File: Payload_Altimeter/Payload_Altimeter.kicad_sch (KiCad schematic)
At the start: 1 part, among them U1 Arduino_Pro_Mini

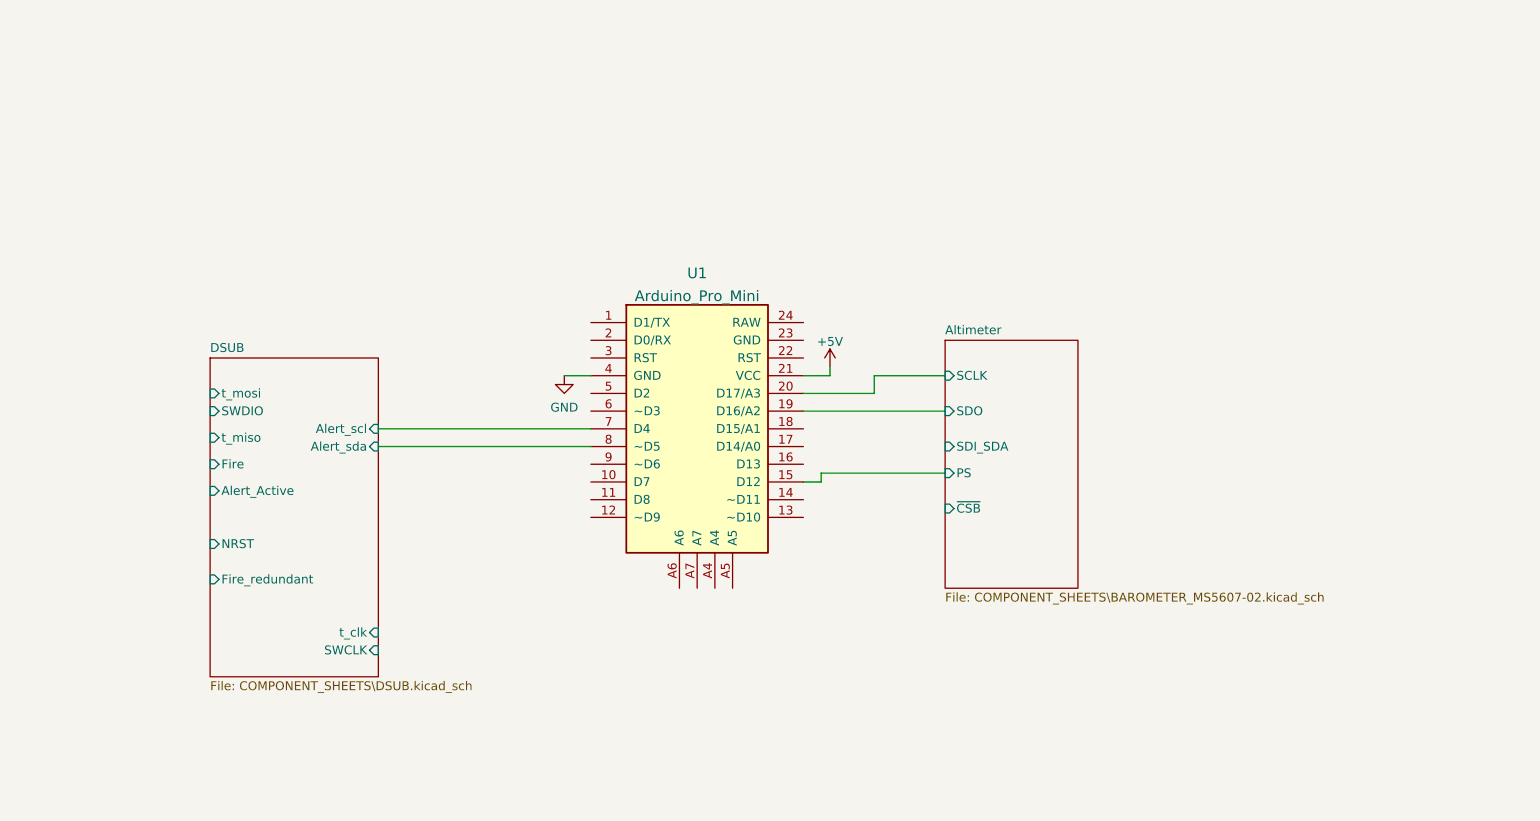
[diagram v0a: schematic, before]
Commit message: Wired 5V created Arduino Sheet
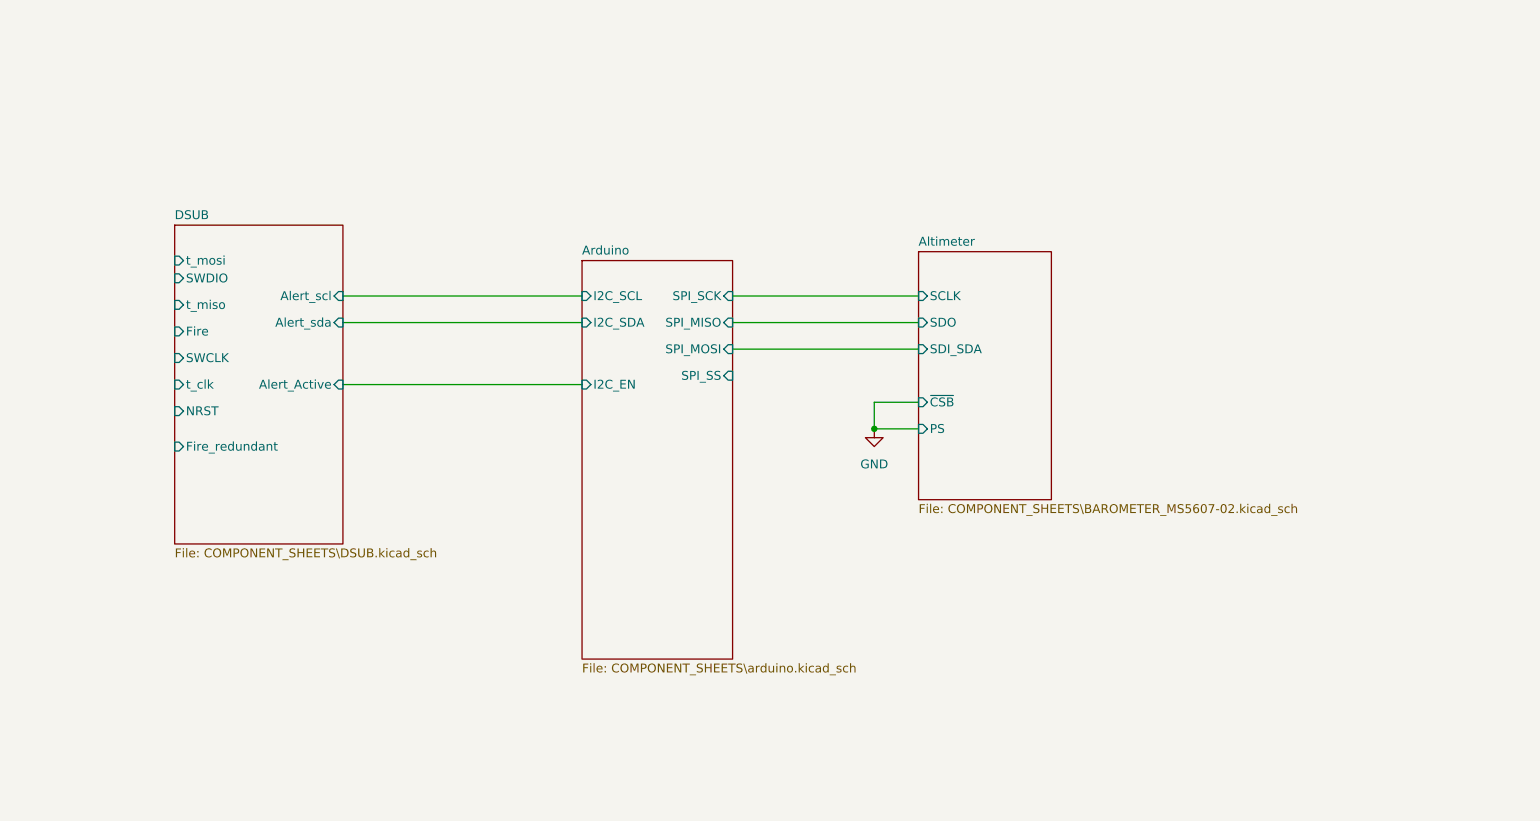
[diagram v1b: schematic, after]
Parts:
- removed U1: Arduino_Pro_Mini, Arduino:Arduino_Pro_Mini, symbol Arduino:Arduino_Pro_Mini
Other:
- added sheet Arduino (COMPONENT_SHEETS\arduino.kicad_sch)

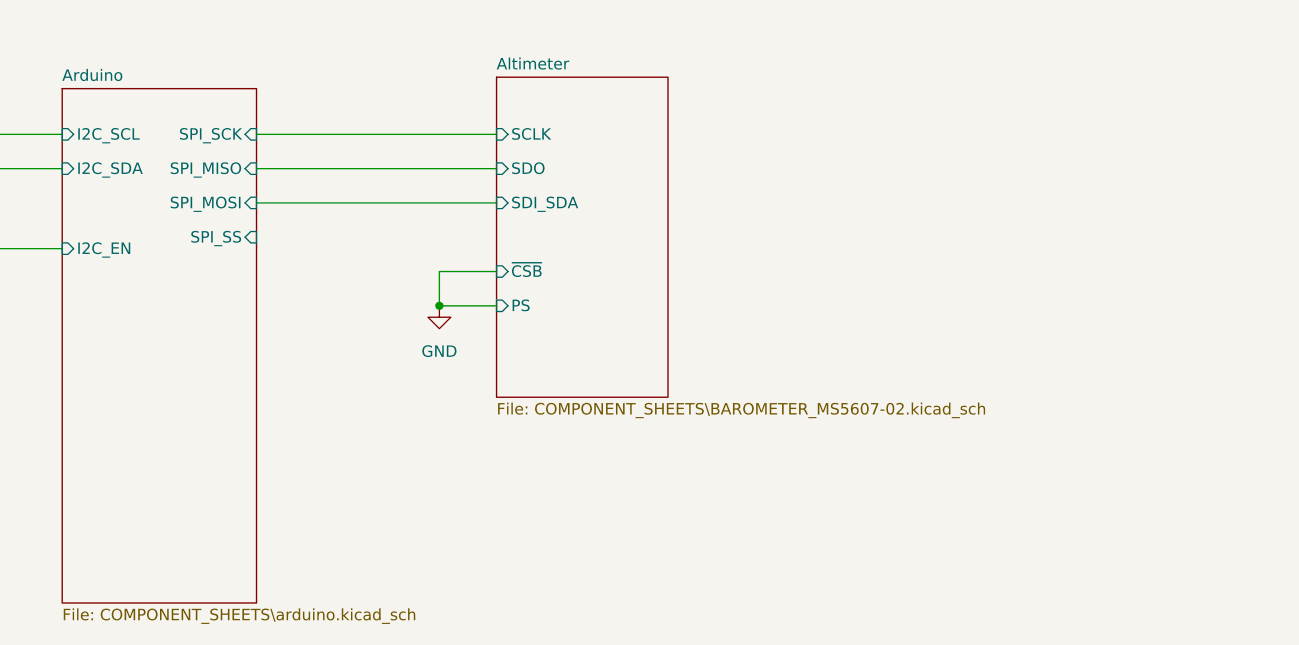
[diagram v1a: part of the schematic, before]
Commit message: added sd card
sd card was added and traces were placed for other components
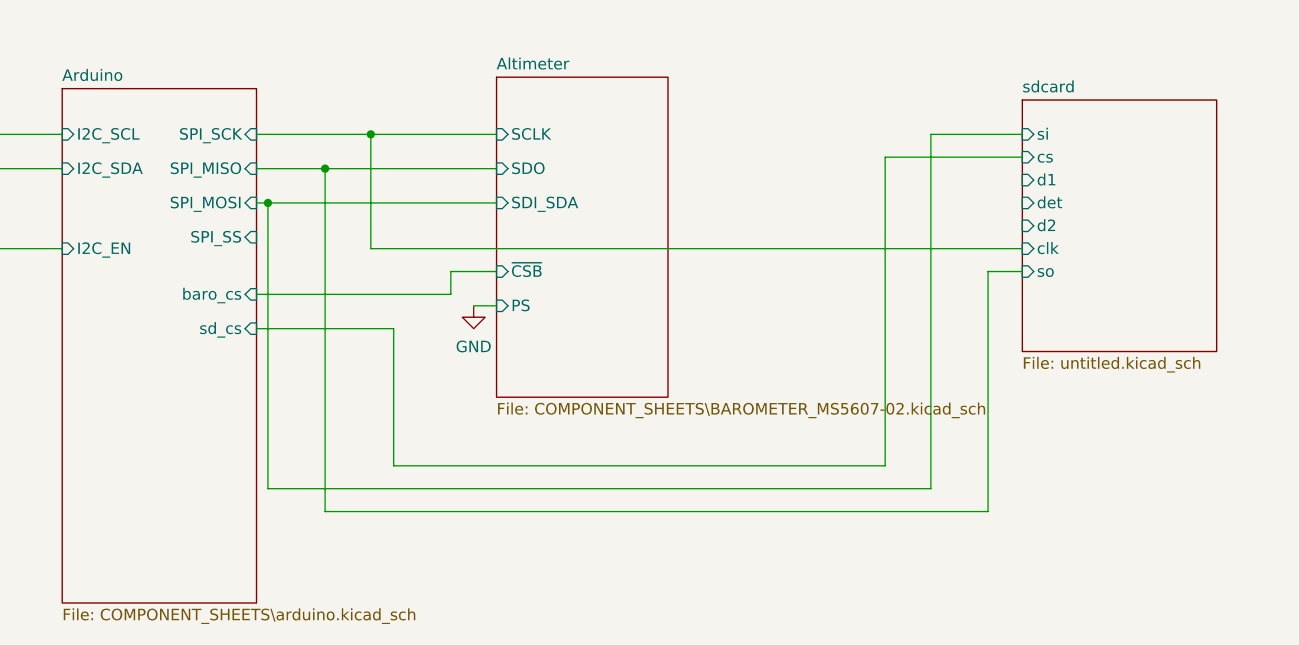
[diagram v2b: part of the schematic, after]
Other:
- added sheet sdcard (untitled.kicad_sch)
- sheet Arduino ports: added baro_cs, sd_cs; removed none
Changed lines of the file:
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@@
 (kicad_sch (version 20211123) (generator eeschema)
   (paper "A4")
-  (junction (at 142.24 90.17) (diameter 0) (color 0 0 0 0)
+  (junction (at 134.62 71.12) (diameter 0) (color 0 0 0 0)
+  )
+  (junction (at 129.54 74.93) (diameter 0) (color 0 0 0 0)
+  )
+  (junction (at 123.19 78.74) (diameter 0) (color 0 0 0 0)
+  )
+  (wire (pts (xy 134.62 71.12) (xy 148.59 71.12))
+    (stroke (width 0) (type default) (color 0 0 0 0))
   )
   (wire (pts (xy 66.04 71.12) (xy 100.33 71.12))
     (stroke (width 0) (type default) (color 0 0 0 0))
   )
-  (wire (pts (xy 142.24 90.17) (xy 148.59 90.17))
-    (stroke (width 0) (type default) (color 0 0 0 0))
-  )
-  (wire (pts (xy 148.59 86.36) (xy 142.24 86.36))
+  (wire (pts (xy 191.77 107.95) (xy 191.77 73.66))
+    (stroke (width 0) (type default) (color 0 0 0 0))
+  )
+  (wire (pts (xy 196.85 110.49) (xy 196.85 71.12))
+    (stroke (width 0) (type default) (color 0 0 0 0))
+  )
+  (wire (pts (xy 143.51 86.36) (xy 148.59 86.36))
+    (stroke (width 0) (type default) (color 0 0 0 0))
+  )
+  (wire (pts (xy 134.62 83.82) (xy 134.62 71.12))
+    (stroke (width 0) (type default) (color 0 0 0 0))
+  )
+  (wire (pts (xy 123.19 110.49) (xy 196.85 110.49))
+    (stroke (width 0) (type default) (color 0 0 0 0))
+  )
+  (wire (pts (xy 123.19 78.74) (xy 123.19 110.49))
+    (stroke (width 0) (type default) (color 0 0 0 0))
+  )
+  (wire (pts (xy 121.92 88.9) (xy 143.51 88.9))
+    (stroke (width 0) (type default) (color 0 0 0 0))
+  )
+  (wire (pts (xy 129.54 74.93) (xy 148.59 74.93))
+    (stroke (width 0) (type default) (color 0 0 0 0))
+  )
+  (wire (pts (xy 207.01 86.36) (xy 203.2 86.36))
+    (stroke (width 0) (type default) (color 0 0 0 0))
+  )
+  (wire (pts (xy 121.92 92.71) (xy 137.16 92.71))
+    (stroke (width 0) (type default) (color 0 0 0 0))
+  )
+  (wire (pts (xy 123.19 78.74) (xy 148.59 78.74))
     (stroke (width 0) (type default) (color 0 0 0 0))
   )
@@
     (stroke (width 0) (type default) (color 0 0 0 0))
   )
-  (wire (pts (xy 121.92 78.74) (xy 148.59 78.74))
-    (stroke (width 0) (type default) (color 0 0 0 0))
-  )
-  (wire (pts (xy 142.24 86.36) (xy 142.24 90.17))
-    (stroke (width 0) (type default) (color 0 0 0 0))
-  )
-  (wire (pts (xy 121.92 74.93) (xy 148.59 74.93))
+  (wire (pts (xy 196.85 71.12) (xy 207.01 71.12))
+    (stroke (width 0) (type default) (color 0 0 0 0))
+  )
+  (wire (pts (xy 143.51 88.9) (xy 143.51 86.36))
+    (stroke (width 0) (type default) (color 0 0 0 0))
+  )
+  (wire (pts (xy 121.92 78.74) (xy 123.19 78.74))
+    (stroke (width 0) (type default) (color 0 0 0 0))
+  )
+  (wire (pts (xy 203.2 113.03) (xy 129.54 113.03))
+    (stroke (width 0) (type default) (color 0 0 0 0))
+  )
+  (wire (pts (xy 129.54 113.03) (xy 129.54 74.93))
+    (stroke (width 0) (type default) (color 0 0 0 0))
+  )
+  (wire (pts (xy 146.05 90.17) (xy 148.59 90.17))
+    (stroke (width 0) (type default) (color 0 0 0 0))
+  )
+  (wire (pts (xy 137.16 92.71) (xy 137.16 107.95))
+    (stroke (width 0) (type default) (color 0 0 0 0))
+  )
+  (wire (pts (xy 137.16 107.95) (xy 191.77 107.95))
+    (stroke (width 0) (type default) (color 0 0 0 0))
+  )
+  (wire (pts (xy 191.77 73.66) (xy 207.01 73.66))
+    (stroke (width 0) (type default) (color 0 0 0 0))
+  )
+  (wire (pts (xy 207.01 83.82) (xy 134.62 83.82))
+    (stroke (width 0) (type default) (color 0 0 0 0))
+  )
+  (wire (pts (xy 121.92 74.93) (xy 129.54 74.93))
     (stroke (width 0) (type default) (color 0 0 0 0))
   )
@@
     (stroke (width 0) (type default) (color 0 0 0 0))
   )
-  (wire (pts (xy 121.92 71.12) (xy 148.59 71.12))
-    (stroke (width 0) (type default) (color 0 0 0 0))
-  )
-  (symbol (lib_id "power:GND") (at 142.24 90.17 0) (unit 1)
+  (wire (pts (xy 121.92 71.12) (xy 134.62 71.12))
+    (stroke (width 0) (type default) (color 0 0 0 0))
+  )
+  (wire (pts (xy 203.2 86.36) (xy 203.2 113.03))
+    (stroke (width 0) (type default) (color 0 0 0 0))
+  )
+  (symbol (lib_id "power:GND") (at 146.05 90.17 0) (unit 1)
     (in_bom yes) (on_board yes) (fields_autoplaced)
-    (property "Reference" "#PWR0101" (id 0) (at 142.24 96.52 0)
+    (property "Reference" "#PWR0101" (id 0) (at 146.05 96.52 0)
       (effects (font (size 1.27 1.27)) hide)
     )
-    (property "Value" "GND" (id 1) (at 142.24 95.25 0))
-    (property "Footprint" "" (id 2) (at 142.24 90.17 0)
+    (property "Value" "GND" (id 1) (at 146.05 94.7325 0))
+    (property "Footprint" "" (id 2) (at 146.05 90.17 0)
       (effects (font (size 1.27 1.27)) hide)
     )
-    (property "Datasheet" "" (id 3) (at 142.24 90.17 0)
+    (property "Datasheet" "" (id 3) (at 146.05 90.17 0)
       (effects (font (size 1.27 1.27)) hide)
     )
@@
       (effects (font (size 1.27 1.27)) (justify right))
     )
+    (pin "baro_cs" input (at 121.92 88.9 0)
+      (effects (font (size 1.27 1.27)) (justify right))
+    )
+    (pin "sd_cs" input (at 121.92 92.71 0)
+      (effects (font (size 1.27 1.27)) (justify right))
+    )
   )
   (sheet (at 148.59 64.77) (size 19.05 35.56) (fields_autoplaced)
@@
     )
   )
+  (sheet (at 207.01 67.31) (size 21.59 27.94) (fields_autoplaced)
+    (stroke (width 0.1524) (type solid) (color 0 0 0 0))
+    (fill (color 0 0 0 0.0000))
+    (property "Sheet name" "sdcard" (id 0) (at 207.01 66.5984 0)
+      (effects (font (size 1.27 1.27)) (justify left bottom))
+    )
+    (property "Sheet file" "untitled.kicad_sch" (id 1) (at 207.01 95.8346 0)
+      (effects (font (size 1.27 1.27)) (justify left top))
+    )
+    (pin "si" input (at 207.01 71.12 180)
+      (effects (font (size 1.27 1.27)) (justify left))
+    )
+    (pin "cs" input (at 207.01 73.66 180)
+      (effects (font (size 1.27 1.27)) (justify left))
+    )
+    (pin "d1" input (at 207.01 76.2 180)
+      (effects (font (size 1.27 1.27)) (justify left))
+    )
+    (pin "det" input (at 207.01 78.74 180)
+      (effects (font (size 1.27 1.27)) (justify left))
+    )
+    (pin "d2" input (at 207.01 81.28 180)
+      (effects (font (size 1.27 1.27)) (justify left))
+    )
+    (pin "clk" input (at 207.01 83.82 180)
+      (effects (font (size 1.27 1.27)) (justify left))
+    )
+    (pin "so" input (at 207.01 86.36 180)
+      (effects (font (size 1.27 1.27)) (justify left))
+    )
+  )
   (sheet_instances
     (path "/" (page "1"))
@@
     (path "/5fba5415-62df-4f11-b066-c862c7f4f614" (page "3"))
     (path "/18be7ca6-5942-4bc1-bf13-c4393b1dbad1" (page "4"))
+    (path "/abdb6179-bbd9-4d88-83fc-0a11cdff4490" (page "5"))
   )
   (symbol_instances
-    (path "/0730ce47-0bea-44a3-992c-5d03f0a08e83/00000000-0000-0000-0000-000061c3cdc8"
-      (reference "#PWR05") (unit 1) (value "+5V") (footprint "")
-    )
     (path "/0730ce47-0bea-44a3-992c-5d03f0a08e83/00000000-0000-0000-0000-000061cfebab"
       (reference "#PWR06") (unit 1) (value "GND") (footprint "")
@@
       (reference "#PWR041") (unit 1) (value "+3.3V") (footprint "")
     )
-    (path "/3173228b-321f-47a8-9f9f-de86f5417cd0"
+    (path "/f1b4ec71-7b55-44c8-84cb-508adfdf4c63"
       (reference "#PWR0101") (unit 1) (value "GND") (footprint "")
     )
@@
       (reference "#PWR0103") (unit 1) (value "GND") (footprint "")
     )
+    (path "/0730ce47-0bea-44a3-992c-5d03f0a08e83/58442b5d-6983-40cc-bc9c-d8f0af4d6d86"
+      (reference "#PWR0104") (unit 1) (value "+5V") (footprint "")
+    )
+    (path "/0730ce47-0bea-44a3-992c-5d03f0a08e83/1d7af2fb-9312-4ce2-9df7-62fb6ef2fa26"
+      (reference "#PWR0105") (unit 1) (value "+5V") (footprint "")
+    )
+    (path "/abdb6179-bbd9-4d88-83fc-0a11cdff4490/b48e6861-adf2-4473-858f-d65f8dcea6c9"
+      (reference "#PWR0106") (unit 1) (value "+3V3") (footprint "")
+    )
+    (path "/abdb6179-bbd9-4d88-83fc-0a11cdff4490/d5954016-c980-4371-a52c-a53007d822f3"
+      (reference "#PWR0107") (unit 1) (value "GND") (footprint "")
+    )
     (path "/5fba5415-62df-4f11-b066-c862c7f4f614/00000000-0000-0000-0000-000061610282"
       (reference "C12") (unit 1) (value "100nF") (footprint "Capacitor_Tantalum_SMD:CP_EIA-3528-15_AVX-H_Pad1.50x2.35mm_HandSolder")
@@
       (reference "J1") (unit 1) (value "L717SDC37P1ACH4F") (footprint "RDT_Custom_Footprints:L717SDC37P1ACH4F")
     )
-    (path "/0730ce47-0bea-44a3-992c-5d03f0a08e83/00000000-0000-0000-0000-000061c3adee"
-      (reference "JP1") (unit 1) (value "5V Disconnect") (footprint "Jumper:SolderJumper-2_P1.3mm_Bridged_Pad1.0x1.5mm")
+    (path "/abdb6179-bbd9-4d88-83fc-0a11cdff4490/71d6f518-fb46-4753-adea-d4368d3f3e26"
+      (reference "J2") (unit 1) (value "Conn_01x09") (footprint "Connector_PinHeader_2.54mm:PinHeader_1x09_P2.54mm_Vertical")
     )
     (path "/18be7ca6-5942-4bc1-bf13-c4393b1dbad1/4ac59da2-094a-4712-84ed-13816bdf2b3f"
